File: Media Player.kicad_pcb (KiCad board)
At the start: 4 copper layers, 114.3 x 68.5 mm, 147 parts, among them J1 12402012E212A, J10 MEM2075-00-140-01-A, J40 PH2.0, J41 UART, J70 PJ-327C-4A, Q10 DMP3068L-7, Q40 DMP3068L-7, Q50 DMP3068L-7, Q70 DMP3068L-7, SW30 BOOT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

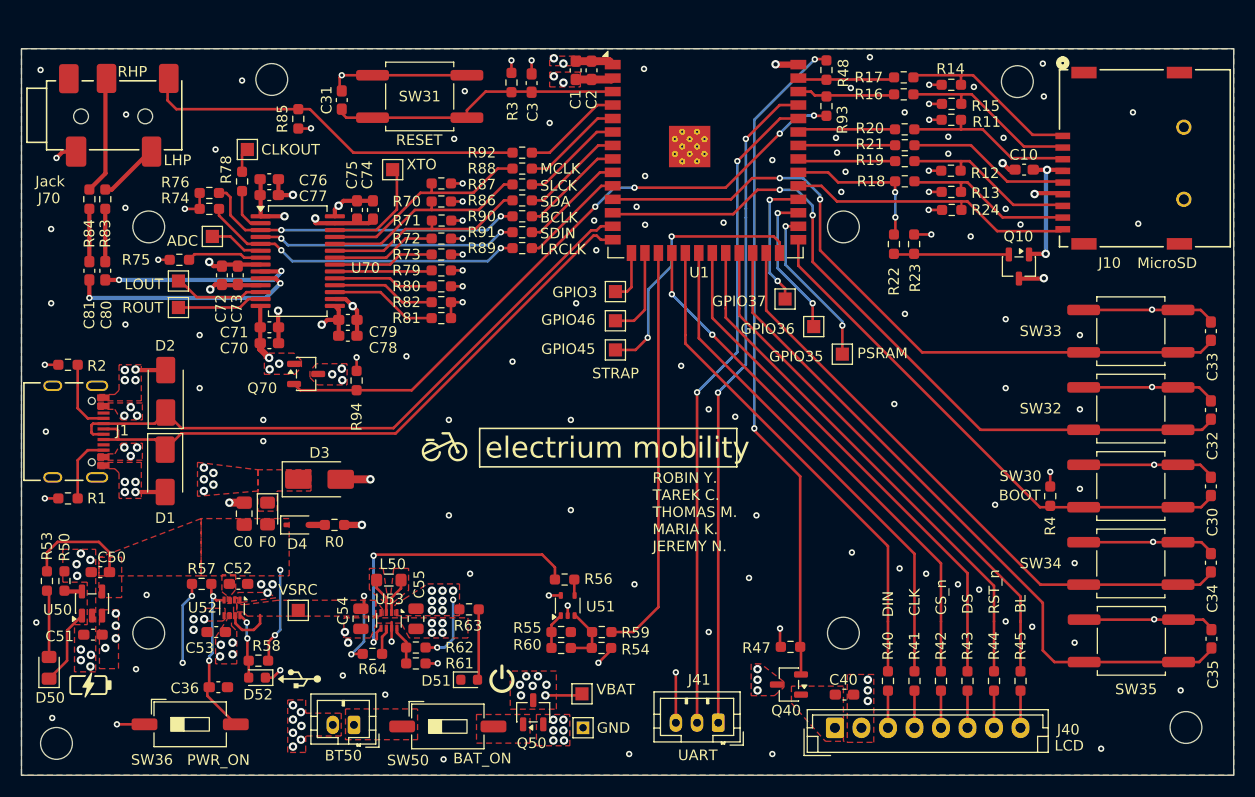
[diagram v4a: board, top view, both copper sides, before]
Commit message: ORDERED: Updated Footprints, Silk Screen, Mounting Holes
Minor changes. This is the version sent to JLC
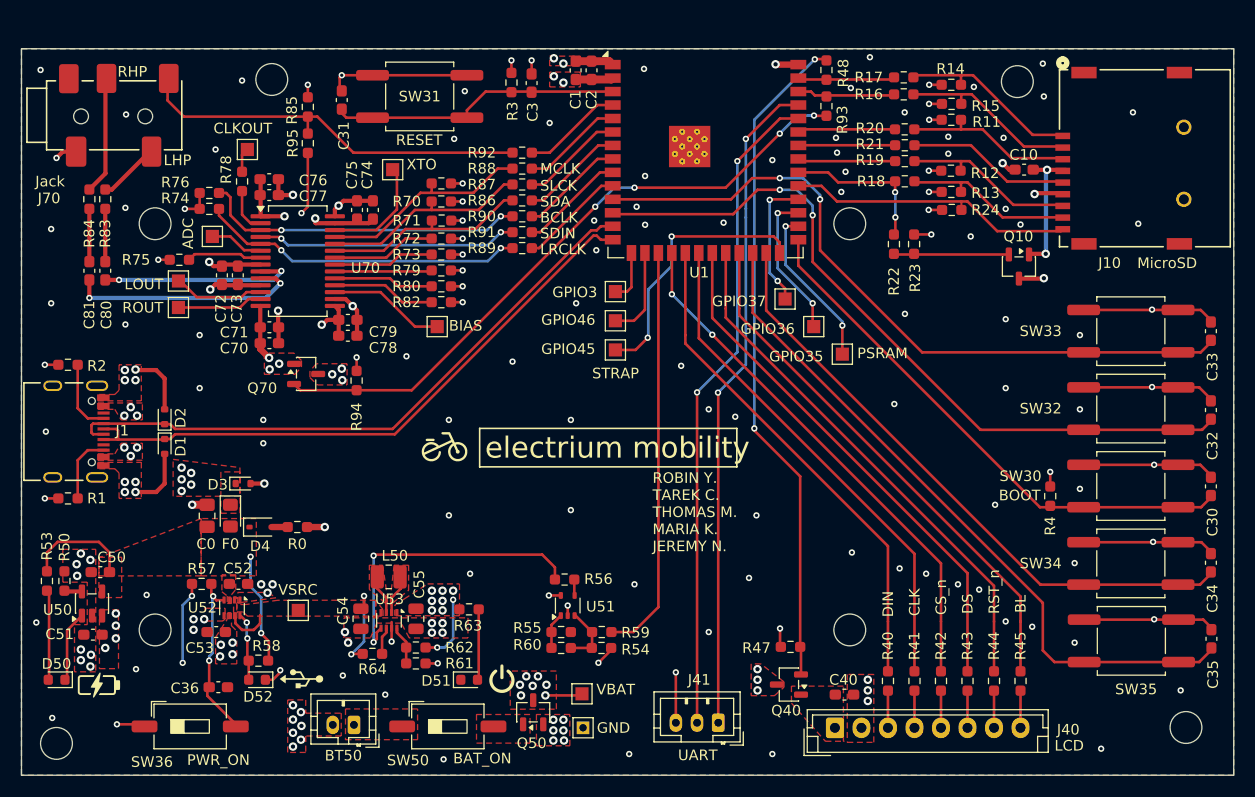
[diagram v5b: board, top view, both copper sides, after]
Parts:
- removed R81: 47kΩ, Resistor_SMD:R_0603_1608Metric_Pad0.98x0.95mm_HandSolder
- added R95: 10kΩ, Resistor_SMD:R_0603_1608Metric_Pad0.98x0.95mm_HandSolder, F.Cu at (113.2, 48.9)
- added TP74: BIAS, footprints:TestPoint_Pad_1.5x1.5mm, F.Cu at (125.4, 66.2)
- D1, D2, D3: footprint Diode_SMD:D_SMA -> Diode_SMD:D_SOD-523
- D50: footprint LED_SMD:LED_0805_2012Metric_Pad1.15x1.40mm_HandSolder -> LED_SMD:LED_0603_1608Metric
- J70: value PJ-327C-4A -> PJ-327A
- L50: value 1uH -> DFE252012P-1R0M=P2; footprint Inductor_SMD:L_0805_2012Metric_Pad1.05x1.20mm_HandSolder -> Inductor_SMD:L_1008_2520Metric
- moved D3 7.21 mm to (107.1, 81.0)
- moved F0 3.51 mm to (105.9, 84.0)
- moved C0 3.51 mm to (103.7, 84.0)
- moved D4 3.51 mm to (108.8, 85.1)
- moved R0 3.51 mm to (112.2, 85.1)
- moved D2 2.40 mm to (99.7, 74.7)
- moved D1 2.30 mm to (99.7, 77.5)
- moved R85 1.44 mm to (113.2, 45.5), turned to 90 degrees
- moved D50 1.33 mm to (89.5, 99.5), turned to 180 degrees
- moved G*** 0.80 mm to (93.5, 100.0)
- moved L50 0.30 mm to (120.8, 89.8)
- moved D52 0.20 mm to (108.4, 99.5)
- moved SW36 0.20 mm to (102.1, 103.9)
- moved G*** 0.20 mm to (112.6, 99.4)
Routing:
- net /AudioAlt/AVDD: track 22.1 -> 28.1 mm, vias 6 -> 7
- net GND: track 149.6 -> 154.5 mm
- net Net-(D50-A): track 6.33 -> 8.81 mm
- net /AudioAlt/A2_TSW: track 36.6 -> 38.2 mm
- net VBUS: track 19.7 -> 21.2 mm
- net /AudioAlt/VMID: track 9.72 -> 8.22 mm
- net Net-(U70-MICBIAS): track 10.1 -> 11.0 mm
- net /USB_D-: track 59.7 -> 58.8 mm
- net /USB_D+: track 58.6 -> 57.8 mm
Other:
- outline, holes or cut-outs redrawn
- board text added: "BIAS"
- board text removed: "Confirm Audio connections --> mainly i2c and microphone VMID stuff Check Silkscreen thickeness Look for floating connections/unnecessary curves on traces Make sure audio jack switch is pulled correctly ASK GPT FOR MORE THINGS TO DOUBLE CHECK pls pls pls double check mounting hole positioning Confirm all IC's are using the right footprints Spend time reading over all datasheets again :sob:"
- board text removed: "Is audio power plane ok? Many obstructions to direction power path"
